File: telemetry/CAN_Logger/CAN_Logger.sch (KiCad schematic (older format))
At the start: 57 parts, among them J1 CONN_02X03, J2 SD_socket, J3 MM_F_RA_20, U1 MCP2561-E_SN, U101 TPS560430YF, U2 ATMEGA16M1, U3 LM3480, U4 TXB0104, U5 R_500, U6 R_500, U7 R_500, Y1 Crystal_SMD

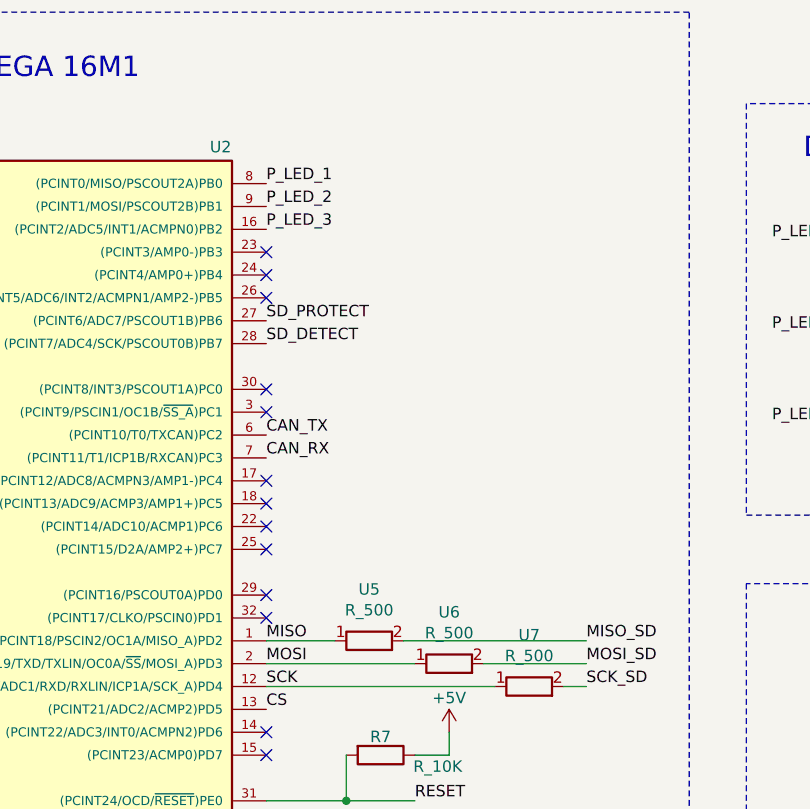
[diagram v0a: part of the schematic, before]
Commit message: Worked PCB Layout, small schematic changes
+Layout: Everything on board, placed some wires and vias
+Schematic: Moved locations of P_LEDs on ATMEGA
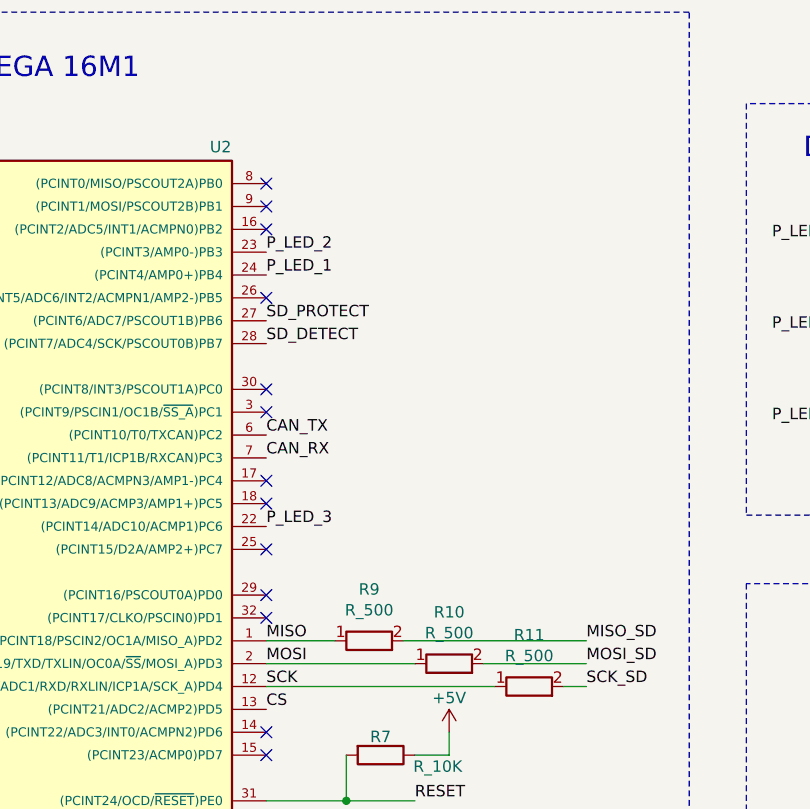
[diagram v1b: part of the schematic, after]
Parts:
- renumbered U6 to R10, U7 to R11, U5 to R9
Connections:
- net P_LED_1: now also U2.24 ((PCINT4/AMP0+)PB4); no longer U2.8 ((PCINT0/MISO/PSCOUT2A)PB0)
- net P_LED_2: now also U2.23 ((PCINT3/AMP0-)PB3); no longer U2.9 ((PCINT1/MOSI/PSCOUT2B)PB1)
- net P_LED_3: now also U2.22 ((PCINT14/ADC10/ACMP1)PC6); no longer U2.16 ((PCINT2/ADC5/INT1/ACMPN0)PB2)
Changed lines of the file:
@@
 	5050 3700 4050 3700
 $Comp
-L formula:R_500 U7
+L formula:R_500 R11
 U 1 1 5FF5E664
 P 5200 3700
-F 0 "U7" H 5200 3925 50  0000 C CNN
+F 0 "R11" H 5200 3925 50  0000 C CNN
 F 1 "R_500" H 5200 3834 50  0000 C CNN
 F 2 "footprints:R_0805_OEM" H 5200 3700 50  0001 C CNN
@@
 $EndComp
 $Comp
-L formula:R_500 U6
+L formula:R_500 R10
 U 1 1 5FF5E1D4
 P 4850 3600
-F 0 "U6" H 4850 3825 50  0000 C CNN
+F 0 "R10" H 4850 3825 50  0000 C CNN
 F 1 "R_500" H 4850 3734 50  0000 C CNN
 F 2 "footprints:R_0805_OEM" H 4850 3600 50  0001 C CNN
@@
 $EndComp
 $Comp
-L formula:R_500 U5
+L formula:R_500 R9
 U 1 1 5FF4CD54
 P 4500 3500
-F 0 "U5" H 4500 3725 50  0000 C CNN
+F 0 "R9" H 4500 3725 50  0000 C CNN
 F 1 "R_500" H 4500 3634 50  0000 C CNN
 F 2 "footprints:R_0805_OEM" H 4500 3500 50  0001 C CNN
@@
 NoConn ~ 4050 3300
 NoConn ~ 4050 3100
-NoConn ~ 4050 3000
+NoConn ~ 4050 1700
 NoConn ~ 4050 2900
 NoConn ~ 4050 2800
 NoConn ~ 4050 2000
-NoConn ~ 4050 1900
-NoConn ~ 4050 1800
+NoConn ~ 4050 1600
+NoConn ~ 4050 1500
 NoConn ~ 4050 2500
 NoConn ~ 4050 2400
-Text Label 4050 1700 0    50   ~ 0
+Text Label 4050 3000 0    50   ~ 0
 P_LED_3
-Text Label 4050 1600 0    50   ~ 0
+Text Label 4050 1800 0    50   ~ 0
 P_LED_2
-Text Label 4050 1500 0    50   ~ 0
+Text Label 4050 1900 0    50   ~ 0
 P_LED_1
 Text Label 4050 2200 0    50   ~ 0
@@
 	10450 3100 12000 3100
 $Comp
-L power:GND #PWR?
+L power:GND #PWR0112
 U 1 1 60394B7B
 P 11400 5750
-F 0 "#PWR?" H 11400 5500 50  0001 C CNN
+F 0 "#PWR0112" H 11400 5500 50  0001 C CNN
 F 1 "GND" H 11405 5577 50  0000 C CNN
 F 2 "" H 11400 5750 50  0001 C CNN

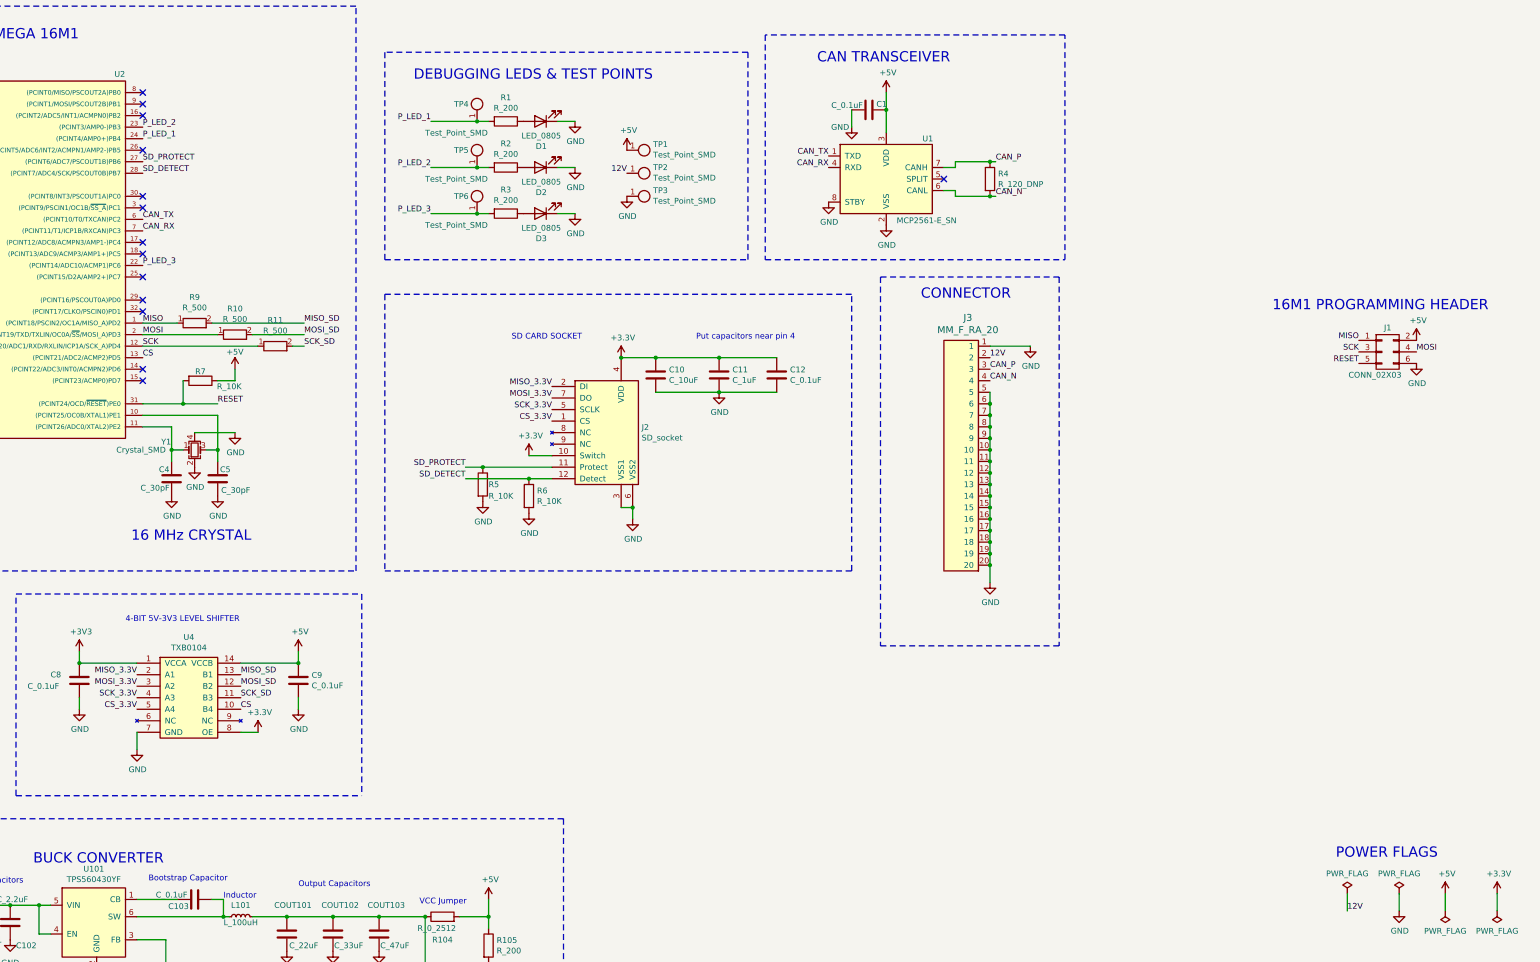
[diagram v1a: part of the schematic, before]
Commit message: Rearranging layout, changed 3.3V to 3V3
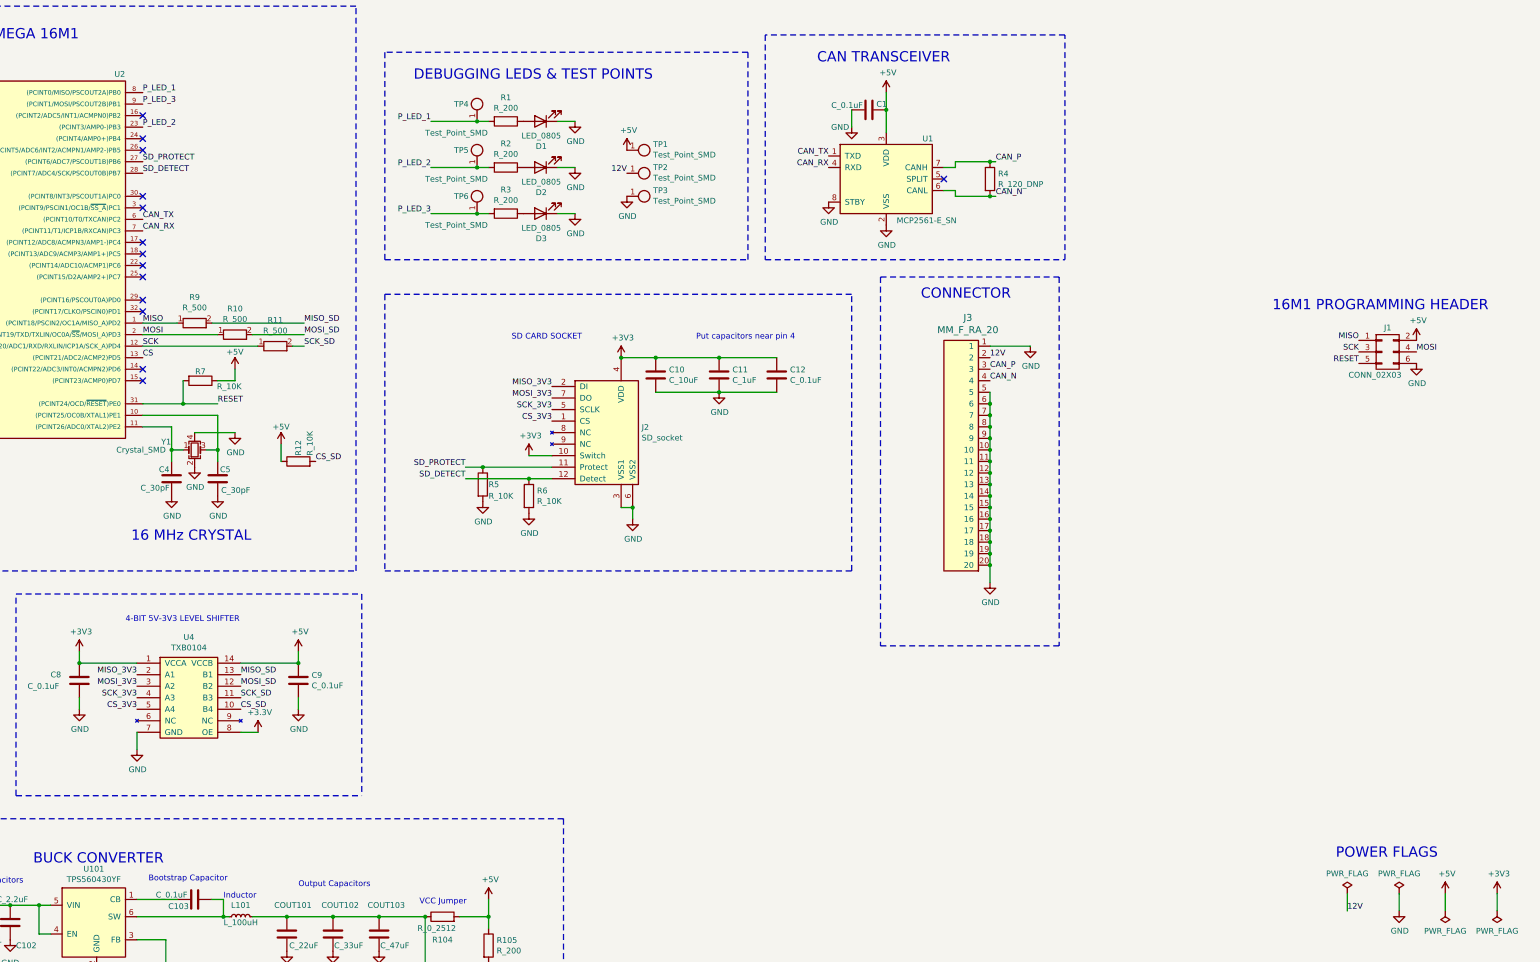
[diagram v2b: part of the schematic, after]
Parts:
- added R12: R_10K, footprints:R_0805_OEM, symbol formula:R_10K
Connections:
- net +5V: now also R12.1
- net CS: no longer U4.10 (B4)
- net P_LED_1: now also U2.8 ((PCINT0/MISO/PSCOUT2A)PB0); no longer U2.24 ((PCINT4/AMP0+)PB4)
- net P_LED_3: now also U2.9 ((PCINT1/MOSI/PSCOUT2B)PB1); no longer U2.22 ((PCINT14/ADC10/ACMP1)PC6)
- net CS_3.3V renamed CS_3V3
- net MISO_3.3V renamed MISO_3V3
- net MOSI_3.3V renamed MOSI_3V3
- net SCK_3.3V renamed SCK_3V3
- new net CS_SD: R12.2, U4.10 (B4)
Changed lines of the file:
@@
 $EndComp
 Text Label 4900 6850 0    50   ~ 0
-CS
+CS_SD
 $Comp
 L formula:C_0.1uF C9
@@
 	3500 6450 3500 6350
 Text Label 4000 6850 2    50   ~ 0
-CS_3.3V
+CS_3V3
 Text Label 4000 6750 2    50   ~ 0
-SCK_3.3V
+SCK_3V3
 Text Label 4000 6650 2    50   ~ 0
-MOSI_3.3V
-Text Label 4000 6550 2    50   ~ 0
-MISO_3.3V
+MOSI_3V3
 $Comp
 L formula:C_0.1uF C8
@@
 Connection ~ 8500 3800
 Wire Wire Line
-	7400 4650 7600 4650
-$Comp
-L power:+3.3V #PWR035
-U 1 1 5FB944A8
-P 7400 4650
-F 0 "#PWR035" H 7400 4500 50  0001 C CNN
-F 1 "+3.3V" H 7415 4823 50  0000 C CNN
-F 2 "" H 7400 4650 50  0001 C CNN
-F 3 "" H 7400 4650 50  0001 C CNN
-	1    7400 4650
-	1    0    0    -1
-$EndComp
-Wire Wire Line
 	8200 3800 8500 3800
 Wire Wire Line
@@
 	1    0    0    -1
 $EndComp
-$Comp
-L power:+3.3V #PWR037
-U 1 1 5FB76E08
-P 8200 3800
-F 0 "#PWR037" H 8200 3650 50  0001 C CNN
-F 1 "+3.3V" H 8215 3973 50  0000 C CNN
-F 2 "" H 8200 3800 50  0001 C CNN
-F 3 "" H 8200 3800 50  0001 C CNN
-	1    8200 3800
-	1    0    0    -1
-$EndComp
 Text Label 7600 4350 2    50   ~ 0
-CS_3.3V
+CS_3V3
 Wire Wire Line
 	11400 2400 11450 2400
@@
 	15350 8450 15350 8600
 Text Label 7600 4050 2    50   ~ 0
-MISO_3.3V
+MISO_3V3
 Text Label 7600 4150 2    50   ~ 0
-MOSI_3.3V
+MOSI_3V3
 Text Label 7600 4250 2    50   ~ 0
-SCK_3.3V
+SCK_3V3
 Text Label 4900 6550 0    50   ~ 0
 MISO_SD
@@
 Wire Wire Line
 	15800 8450 15800 8600
-$Comp
-L power:+3.3V #PWR0102
-U 1 1 602DE8A6
-P 15800 8450
-F 0 "#PWR0102" H 15800 8300 50  0001 C CNN
-F 1 "+3.3V" H 15815 8623 50  0000 C CNN
-F 2 "" H 15800 8450 50  0001 C CNN
-F 3 "" H 15800 8450 50  0001 C CNN
-	1    15800 8450
-	1    0    0    -1
-$EndComp
 Wire Wire Line
 	1550 1500 1850 1500
@@
 NoConn ~ 4050 2800
 NoConn ~ 4050 2000
-NoConn ~ 4050 1600
-NoConn ~ 4050 1500
 NoConn ~ 4050 2500
 NoConn ~ 4050 2400
-Text Label 4050 3000 0    50   ~ 0
+Text Label 4050 1600 0    50   ~ 0
 P_LED_3
 Text Label 4050 1800 0    50   ~ 0
 P_LED_2
-Text Label 4050 1900 0    50   ~ 0
+Text Label 4050 1500 0    50   ~ 0
 P_LED_1
 Text Label 4050 2200 0    50   ~ 0
@@
 Text Label 4050 2100 0    50   ~ 0
 SD_PROTECT
-Text Label 4050 3800 0    50   ~ 0
-CS
+Text Label 5550 4700 0    50   ~ 0
+CS_SD
 Wire Wire Line
 	4700 4000 4850 4000
@@
 Text Notes 6400 1400 0    89   ~ 0
 DEBUGGING LEDS & TEST POINTS
-Connection ~ 8200 3800
 Connection ~ 7400 4850
 Wire Wire Line
@@
 $EndComp
 Wire Notes Line
-	7700 7800 7700 10350
-Wire Notes Line
 	1000 7800 1000 10350
-Wire Notes Line
-	7700 7800 1000 7800
 Wire Notes Line
 	1000 10350 7700 10350
@@
 	11400 4200 11400 4100
 Connection ~ 11400 4200
+$Comp
+L formula:R_10K R12
+U 1 1 6061ED8A
+P 5400 4700
+F 0 "R12" H 5450 4700 50  0000 L CNN
+F 1 "R_10K" H 5450 4600 50  0000 L CNN
+F 2 "footprints:R_0805_OEM" H 5330 4700 50  0001 C CNN
+F 3 "" H 5480 4700 50  0001 C CNN
+F 4 "DK" H 5400 4700 60  0001 C CNN "MFN"
+F 5 "CRS0805-FX-1002ELFCT-ND" H 5400 4700 60  0001 C CNN "MPN"
+F 6 "https://www.digikey.com/products/en?keywords=CRS0805-FX-1002ELFCT-ND" H 5880 5100 60  0001 C CNN "PurchasingLink"
+	1    5400 4700
+	0    -1   -1   0
+$EndComp
+$Comp
+L power:+5V #PWR021
+U 1 1 606B653B
+P 5250 4550
+F 0 "#PWR021" H 5250 4400 50  0001 C CNN
+F 1 "+5V" H 5250 4700 50  0000 C CNN
+F 2 "" H 5250 4550 50  0001 C CNN
+F 3 "" H 5250 4550 50  0001 C CNN
+	1    5250 4550
+	1    0    0    -1
+$EndComp
+Wire Wire Line
+	5250 4700 5250 4550
+$Comp
+L power:+3V3 #PWR0102
+U 1 1 60542B3E
+P 8200 3800
+F 0 "#PWR0102" H 8200 3650 50  0001 C CNN
+F 1 "+3V3" H 8215 3973 50  0000 C CNN
+F 2 "" H 8200 3800 50  0001 C CNN
+F 3 "" H 8200 3800 50  0001 C CNN
+	1    8200 3800
+	1    0    0    -1
+$EndComp
+Connection ~ 8200 3800
+Text Label 4000 6550 2    50   ~ 0
+MISO_3V3
+$Comp
+L power:+3V3 #PWR0114
+U 1 1 60557034
+P 7400 4650
+F 0 "#PWR0114" H 7400 4500 50  0001 C CNN
+F 1 "+3V3" H 7415 4823 50  0000 C CNN
+F 2 "" H 7400 4650 50  0001 C CNN
+F 3 "" H 7400 4650 50  0001 C CNN
+	1    7400 4650
+	1    0    0    -1
+$EndComp
+Wire Wire Line
+	7600 4650 7400 4650
+Wire Notes Line
+	7700 7800 1000 7800
+Wire Notes Line
+	7700 7800 7700 10350
+$Comp
+L power:+3V3 #PWR0115
+U 1 1 6058846A
+P 15800 8450
+F 0 "#PWR0115" H 15800 8300 50  0001 C CNN
+F 1 "+3V3" H 15815 8623 50  0000 C CNN
+F 2 "" H 15800 8450 50  0001 C CNN
+F 3 "" H 15800 8450 50  0001 C CNN
+	1    15800 8450
+	1    0    0    -1
+$EndComp
+Text Label 4050 3800 0    50   ~ 0
+CS
+NoConn ~ 4050 1900
+NoConn ~ 4050 3000
 $EndSCHEMATC

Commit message: Small tweaks for fabbing
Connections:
- net CS is gone; now on net CS_SD: U2.13 ((PCINT21/ADC2/ACMP2)PD5)
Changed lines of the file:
@@
 $EndComp
 Text Label 4050 3800 0    50   ~ 0
-CS
+CS_SD
 NoConn ~ 4050 1900
 NoConn ~ 4050 3000
